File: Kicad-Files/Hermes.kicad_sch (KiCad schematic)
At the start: 14 parts, among them J1 Conn_01x04_Socket, J2 Conn_01x01_Pin, J3 Conn_01x01_Pin, U1 XIAO-RP2040-DIP, U2 VL53L1CXV0FY1

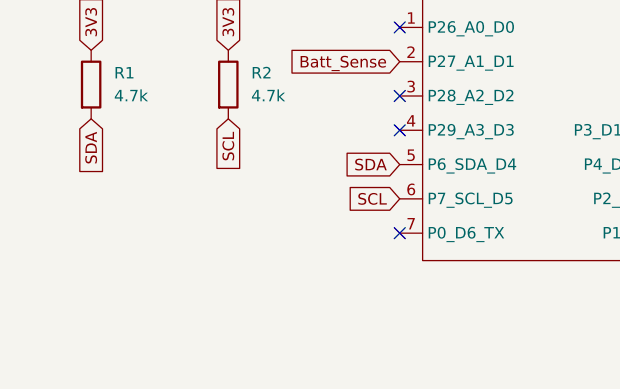
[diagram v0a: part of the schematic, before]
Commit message: Fix BOM update files and add a button to the pcb
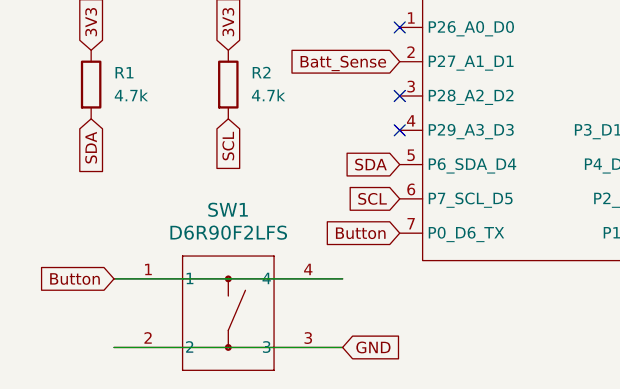
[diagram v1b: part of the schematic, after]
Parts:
- added SW1: D6R90F2LFS, D6R90_CNK, symbol D6R90 F2 LFS:D6R90F2LFS
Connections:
- net GND: now also SW1.2, SW1.3
- net Button: now reaches U1.7 (P0_D6_TX)
- net Button: now also SW1.1, SW1.4
- no-connect marks 6 -> 5
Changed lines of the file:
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@@
-	)
-	(no_connect
-		(at 138.43 143.51)
 	)
 	(no_connect
@@
 	(wire
 		(pts
-			(xy 204.47 123.19) (xy 191.77 123.19)
+			(xy 106.68 156.21) (xy 132.08 156.21)
 		)
 		(stroke
@@
 	(wire
 		(pts
-			(xy 205.74 143.51) (xy 205.74 140.97)
+			(xy 106.68 148.59) (xy 132.08 148.59)
 		)
 		(stroke
@@
 		)
 	)
+	(wire
+		(pts
+			(xy 204.47 123.19) (xy 191.77 123.19)
+		)
+		(stroke
+			(width 0)
+			(type default)
+		)
+	)
+	(wire
+		(pts
+			(xy 205.74 143.51) (xy 205.74 140.97)
+		)
+		(stroke
+			(width 0)
+			(type default)
+		)
+	)
 	(global_label "Sensor"
 		(shape input)
@@
 		)
 	)
+	(global_label "GND"
+		(shape input)
+		(at 132.08 156.21 0)
+		(fields_autoplaced yes)
+		(effects
+			(font
+				(size 1.27 1.27)
+			)
+			(justify left)
+		)
+		(property "Intersheetrefs" "${INTERSHEET_REFS}"
+			(at 138.9357 156.21 0)
+			(effects
+				(font
+					(size 1.27 1.27)
+				)
+				(justify left)
+				(hide yes)
+			)
+		)
+	)
 	(global_label "Batt_NEG"
 		(shape input)
@@
 		)
 	)
+	(global_label "Button"
+		(shape input)
+		(at 106.68 148.59 180)
+		(fields_autoplaced yes)
+		(effects
+			(font
+				(size 1.27 1.27)
+			)
+			(justify right)
+		)
+		(property "Intersheetrefs" "${INTERSHEET_REFS}"
+			(at 97.5264 148.59 0)
+			(effects
+				(font
+					(size 1.27 1.27)
+				)
+				(justify right)
+				(hide yes)
+			)
+		)
+	)
 	(global_label "3V3"
 		(shape input)
@@
 				)
 				(justify left)
+				(hide yes)
+			)
+		)
+	)
+	(global_label "Button"
+		(shape input)
+		(at 138.43 143.51 180)
+		(fields_autoplaced yes)
+		(effects
+			(font
+				(size 1.27 1.27)
+			)
+			(justify right)
+		)
+		(property "Intersheetrefs" "${INTERSHEET_REFS}"
+			(at 129.2764 143.51 0)
+			(effects
+				(font
+					(size 1.27 1.27)
+				)
+				(justify right)
 				(hide yes)
 			)
@@
 					(unit 1)
 				)
+			)
+		)
+	)
+	(symbol
+		(lib_id "D6R90 F2 LFS:D6R90F2LFS")
+		(at 106.68 148.59 0)
+		(unit 1)
+		(exclude_from_sim no)
+		(in_bom yes)
+		(on_board yes)
+		(dnp no)
+		(fields_autoplaced yes)
+		(property "Reference" "SW1"
+			(at 119.38 140.97 0)
+			(effects
+				(font
+					(size 1.524 1.524)
+				)
+			)
+		)
+		(property "Value" "D6R90F2LFS"
+			(at 119.38 143.51 0)
+			(effects
+				(font
+					(size 1.524 1.524)
+				)
+			)
+		)
+		(property "Footprint" "D6R90_CNK"
+			(at 106.68 148.59 0)
+			(effects
+				(font
+					(size 1.27 1.27)
+					(italic yes)
+				)
+				(hide yes)
+			)
+		)
+		(property "Datasheet" "D6R90F2LFS"
+			(at 106.68 148.59 0)
+			(effects
+				(font
+					(size 1.27 1.27)
+					(italic yes)
+				)
+				(hide yes)
+			)
+		)
+		(property "Description" ""
+			(at 106.68 148.59 0)
+			(effects
+				(font
+					(size 1.27 1.27)
+				)
+				(hide yes)
+			)
+		)
+		(pin "4"
+		)
+		(pin "3"
+		)
+		(pin "1"
+		)
+		(pin "2"
+		)
+		(instances
+			(project ""
+				(path "/19245d2f-292e-40b6-bf17-043704df1fae"
+					(reference "SW1")
+					(unit 1)
+				)
